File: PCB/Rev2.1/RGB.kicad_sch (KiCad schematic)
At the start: 64 parts

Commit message: rgb封装调整，加高焊盘并设置实习铺铜
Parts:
- RGB1, RGB10, RGB11, RGB12, RGB13, RGB14, RGB15, RGB16, RGB17, RGB18, RGB19, RGB2, RGB20, RGB21, RGB22, RGB23, RGB24, RGB25, RGB26, RGB27, RGB28, RGB29, RGB3, RGB30, RGB31, RGB32, RGB33, RGB34, RGB35, RGB36, RGB37, RGB38, RGB39, RGB4, RGB40, RGB41, RGB42, RGB43, RGB44, RGB45, RGB46, RGB47, RGB48, RGB49, RGB5, RGB50, RGB51, RGB52, RGB53, RGB54, RGB55, RGB56, RGB57, RGB58, RGB59, RGB6, RGB60, RGB61, RGB7, RGB8, RGB9: footprint RGB:ws2812B_6028_Production -> RGB:ws2812B_6028_Production_EX

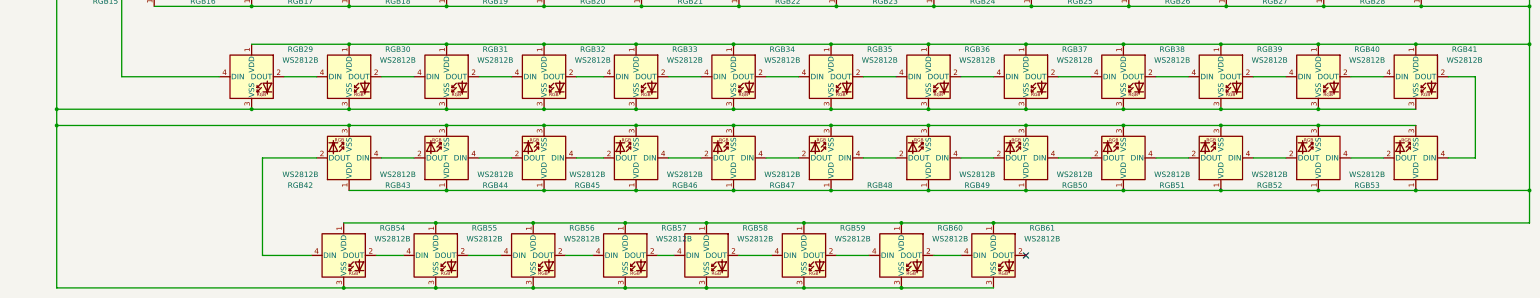
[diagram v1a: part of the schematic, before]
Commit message: 布局调整，rgb，轴座调整，注意二极管位置为手动校准
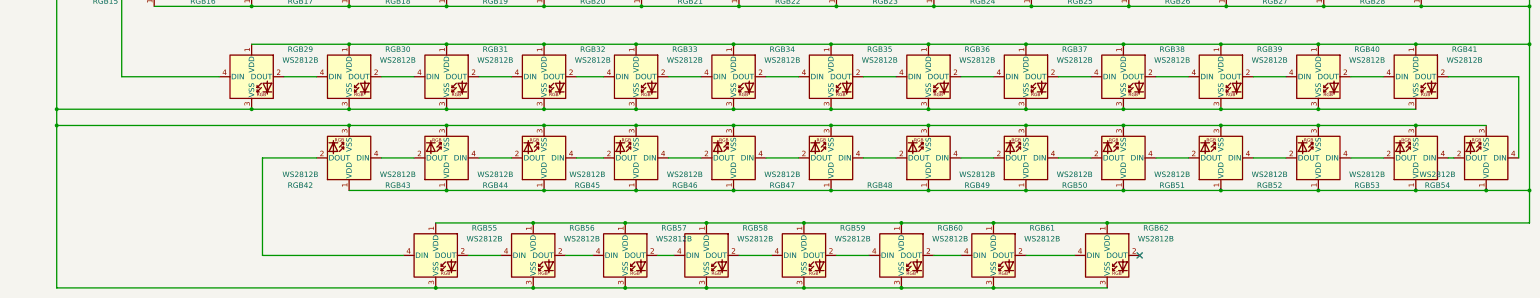
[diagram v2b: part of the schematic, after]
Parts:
- added RGB62: WS2812B, RGB:ws2812B_6028_Production_EX, symbol LED:WS2812B
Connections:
- net GND: now also RGB62.3 (VSS)
- net RGB_VDD: now also RGB62.1 (VDD)
- net at RGB53.4 (DIN): now also RGB54.2 (DOUT); no longer RGB41.2 (DOUT)
- net at RGB55.4 (DIN): now also RGB42.2 (DOUT); no longer RGB54.2 (DOUT)
- net at RGB54.4 (DIN): now also RGB41.2 (DOUT); no longer RGB42.2 (DOUT)
- net at RGB61.2 (DOUT): now also RGB62.4 (DIN)
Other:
- moved on the sheet: RGB54
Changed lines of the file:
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@@
 	)
 	(junction
+		(at 369.57 154.94)
+		(diameter 0)
+		(color 0 0 0 0)
+	)
+	(junction
 		(at 278.13 154.94)
 		(diameter 0)
@@
 	)
 	(junction
-		(at 139.7 177.8)
-		(diameter 0)
-		(color 0 0 0 0)
-	)
-	(junction
 		(at 91.44 40.64)
 		(diameter 0)
@@
 	)
 	(junction
-		(at 118.11 193.04)
-		(diameter 0)
-		(color 0 0 0 0)
-	)
-	(junction
 		(at 119.38 151.13)
 		(diameter 0)
@@
 	)
 	(junction
+		(at 297.18 177.8)
+		(diameter 0)
+		(color 0 0 0 0)
+	)
+	(junction
 		(at 302.26 111.76)
 		(diameter 0)
@@
 	)
 	(junction
+		(at 386.08 170.18)
+		(diameter 0)
+		(color 0 0 0 0)
+	)
+	(junction
 		(at 255.27 170.18)
 		(diameter 0)
@@
 	)
 	(junction
+		(at 270.51 193.04)
+		(diameter 0)
+		(color 0 0 0 0)
+	)
+	(junction
 		(at 232.41 151.13)
 		(diameter 0)
@@
 	)
 	(no_connect
-		(at 278.13 185.42)
+		(at 304.8 185.42)
 	)
 	(wire
@@
 	(wire
 		(pts
-			(xy 396.24 170.18) (xy 369.57 170.18)
+			(xy 396.24 170.18) (xy 386.08 170.18)
 		)
 		(stroke
@@
 	(wire
 		(pts
+			(xy 377.19 162.56) (xy 378.46 162.56)
+		)
+		(stroke
+			(width 0)
+			(type default)
+		)
+	)
+	(wire
+		(pts
 			(xy 279.4 127) (xy 302.26 127)
 		)
@@
 	(wire
 		(pts
-			(xy 118.11 193.04) (xy 50.8 193.04)
+			(xy 50.8 193.04) (xy 139.7 193.04)
 		)
 		(stroke
@@
 	(wire
 		(pts
+			(xy 369.57 154.94) (xy 386.08 154.94)
+		)
+		(stroke
+			(width 0)
+			(type default)
+		)
+	)
+	(wire
+		(pts
 			(xy 346.71 170.18) (xy 369.57 170.18)
 		)
@@
 	(wire
 		(pts
-			(xy 118.11 177.8) (xy 139.7 177.8)
-		)
-		(stroke
-			(width 0)
-			(type default)
-		)
-	)
-	(wire
-		(pts
 			(xy 142.24 170.18) (xy 165.1 170.18)
 		)
@@
 	(wire
 		(pts
-			(xy 125.73 185.42) (xy 132.08 185.42)
-		)
-		(stroke
-			(width 0)
-			(type default)
-		)
-	)
-	(wire
-		(pts
 			(xy 255.27 170.18) (xy 278.13 170.18)
 		)
@@
 	(wire
 		(pts
-			(xy 99.06 185.42) (xy 110.49 185.42)
+			(xy 99.06 185.42) (xy 132.08 185.42)
 		)
 		(stroke
@@
 	(wire
 		(pts
+			(xy 278.13 185.42) (xy 289.56 185.42)
+		)
+		(stroke
+			(width 0)
+			(type default)
+		)
+	)
+	(wire
+		(pts
 			(xy 378.46 99.06) (xy 378.46 119.38)
 		)
@@
 	(wire
 		(pts
+			(xy 297.18 177.8) (xy 396.24 177.8)
+		)
+		(stroke
+			(width 0)
+			(type default)
+		)
+	)
+	(wire
+		(pts
 			(xy 232.41 135.89) (xy 255.27 135.89)
 		)
@@
 	(wire
 		(pts
-			(xy 383.54 162.56) (xy 377.19 162.56)
+			(xy 104.14 143.51) (xy 111.76 143.51)
 		)
 		(stroke
@@
 	(wire
 		(pts
-			(xy 104.14 143.51) (xy 111.76 143.51)
+			(xy 393.7 162.56) (xy 393.7 143.51)
 		)
 		(stroke
@@
 	(wire
 		(pts
-			(xy 118.11 193.04) (xy 139.7 193.04)
-		)
-		(stroke
-			(width 0)
-			(type default)
-		)
-	)
-	(wire
-		(pts
 			(xy 302.26 111.76) (xy 325.12 111.76)
 		)
@@
 	(wire
 		(pts
-			(xy 383.54 143.51) (xy 383.54 162.56)
+			(xy 287.02 99.06) (xy 294.64 99.06)
 		)
 		(stroke
@@
 	(wire
 		(pts
-			(xy 287.02 99.06) (xy 294.64 99.06)
+			(xy 331.47 162.56) (xy 339.09 162.56)
 		)
 		(stroke
@@
 	(wire
 		(pts
-			(xy 331.47 162.56) (xy 339.09 162.56)
+			(xy 270.51 193.04) (xy 297.18 193.04)
 		)
 		(stroke
@@
 	(wire
 		(pts
-			(xy 270.51 177.8) (xy 396.24 177.8)
+			(xy 270.51 177.8) (xy 297.18 177.8)
 		)
 		(stroke
@@
 	(wire
 		(pts
+			(xy 386.08 170.18) (xy 369.57 170.18)
+		)
+		(stroke
+			(width 0)
+			(type default)
+		)
+	)
+	(wire
+		(pts
 			(xy 279.4 111.76) (xy 302.26 111.76)
 		)
@@
 	(wire
 		(pts
-			(xy 377.19 143.51) (xy 383.54 143.51)
+			(xy 377.19 143.51) (xy 393.7 143.51)
 		)
 		(stroke
@@
 	(symbol
 		(lib_id "LED:WS2812B")
-		(at 118.11 185.42 0)
+		(at 386.08 162.56 180)
 		(unit 1)
 		(body_style 1)
@@
 		(dnp no)
 		(property "Reference" "RGB54"
-			(at 129.54 178.9998 0)
+			(at 374.65 168.9802 0)
 			(show_name no)
 			(do_not_autoplace no)
@@
 		)
 		(property "Value" "WS2812B"
-			(at 129.54 181.5398 0)
+			(at 374.65 166.4402 0)
 			(show_name no)
 			(do_not_autoplace no)
@@
 		)
 		(property "Footprint" "RGB:ws2812B_6028_Production_EX"
-			(at 119.38 193.04 0)
+			(at 384.81 154.94 0)
 			(hide yes)
 			(show_name no)
@@
 		)
 		(property "Datasheet" "https://cdn-shop.adafruit.com/datasheets/WS2812B.pdf"
-			(at 120.65 194.945 0)
+			(at 383.54 153.035 0)
 			(hide yes)
 			(show_name no)
@@
 		)
 		(property "Description" "RGB LED with integrated controller"
-			(at 118.11 185.42 0)
+			(at 386.08 162.56 0)
 			(hide yes)
 			(show_name no)
@@
 					(unit 1)
 				)
+			)
+		)
+	)
+	(symbol
+		(lib_id "LED:WS2812B")
+		(at 297.18 185.42 0)
+		(unit 1)
+		(body_style 1)
+		(exclude_from_sim no)
+		(in_bom yes)
+		(on_board yes)
+		(in_pos_files yes)
+		(dnp no)
+		(property "Reference" "RGB62"
+			(at 308.61 178.9998 0)
+			(show_name no)
+			(do_not_autoplace no)
+			(effects
+				(font
+					(size 1.27 1.27)
+				)
+			)
+		)
+		(property "Value" "WS2812B"
+			(at 308.61 181.5398 0)
+			(show_name no)
+			(do_not_autoplace no)
+			(effects
+				(font
+					(size 1.27 1.27)
+				)
+			)
+		)
+		(property "Footprint" "RGB:ws2812B_6028_Production_EX"
+			(at 298.45 193.04 0)
+			(hide yes)
+			(show_name no)
+			(do_not_autoplace no)
+			(effects
+				(font
+					(size 1.27 1.27)
+				)
+				(justify left top)
+			)
+		)
+		(property "Datasheet" "https://cdn-shop.adafruit.com/datasheets/WS2812B.pdf"
+			(at 299.72 194.945 0)
+			(hide yes)
+			(show_name no)
+			(do_not_autoplace no)
+			(effects
+				(font
+					(size 1.27 1.27)
+				)
+				(justify left top)
+			)
+		)
+		(property "Description" "RGB LED with integrated controller"
+			(at 297.18 185.42 0)
+			(hide yes)
+			(show_name no)
+			(do_not_autoplace no)
+			(effects
+				(font
+					(size 1.27 1.27)
+				)
+			)
+		)
+		(pin "2"
+		)
+		(pin "1"
+		)
+		(pin "3"
+		)
+		(pin "4"
+		)
+		(instances
+			(project "PH60-SC_Rev2.1"
+				(path "/dca0f898-8fdb-4522-a51d-f4f4238906e7/972fcb42-aba7-427d-9ffc-eb5767ba1d3c"
+					(reference "RGB62")
+					(unit 1)
+				)
